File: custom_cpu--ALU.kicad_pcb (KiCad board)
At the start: 2 copper layers, 100 x 60 mm, 25 parts, among them J1 CONN_01X08, J10 CONN_01X01, J11 CONN_01X01, J12 CONN_01X01, J2 CONN_01X08, J3 CONN_01X01, J4 CONN_01X01, J5 CONN_01X08, J6 CONN_01X01, J7 CONN_01X01, J8 CONN_01X01, J9 CONN_01X01, U1 74LS283, U2 74LS283, U3 74LS86, U4 74LS86, U5 74LS245

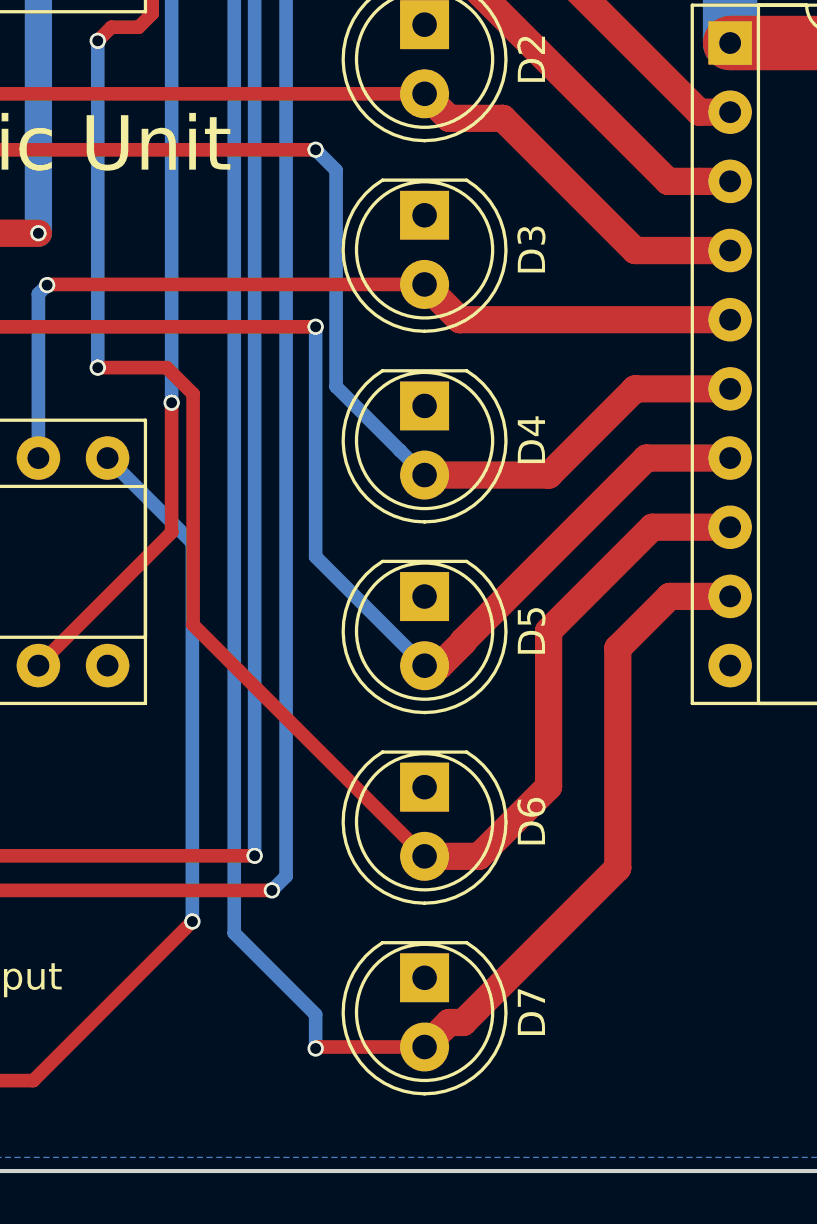
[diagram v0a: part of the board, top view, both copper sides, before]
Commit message: fix a couple more touching traces
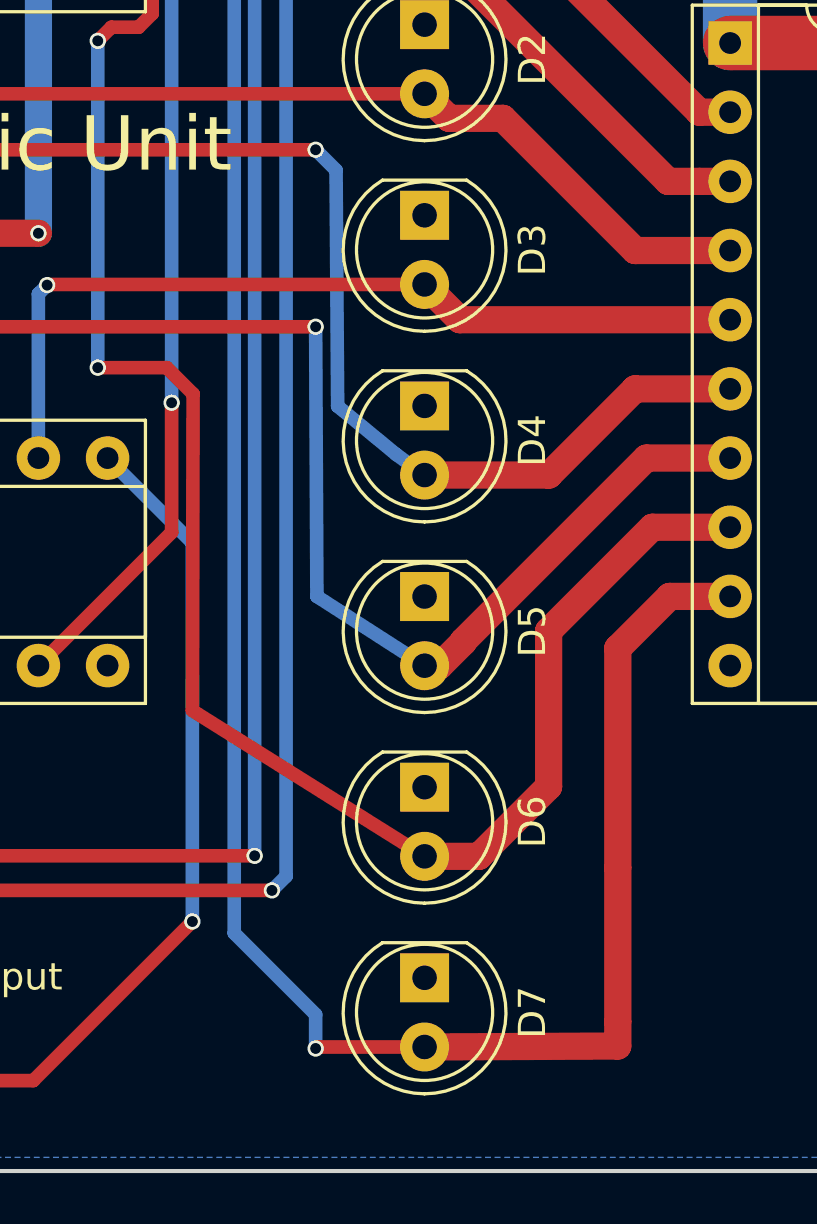
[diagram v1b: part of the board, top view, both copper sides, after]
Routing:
- net Net-(D7-Pad2): track 88.1 -> 91.9 mm
- net Net-(D6-Pad2): track 85.9 -> 87.0 mm
- net Net-(D5-Pad2): track 76.8 -> 77.3 mm
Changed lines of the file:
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@@
-(kicad_pcb (version 4) (host pcbnew 4.0.6-e0-6349~53~ubuntu16.04.1)
+(kicad_pcb (version 4) (host pcbnew 4.0.4+e1-6308~48~ubuntu16.04.1-stable)
   (general
     (links 83)
@@
   )
   (setup
-    (last_trace_width 1)
+    (last_trace_width 0.25)
     (user_trace_width 0.25)
     (user_trace_width 0.5)
@@
   (segment (start 119.295 78.74) (end 129.22 78.74) (width 1) (layer F.Cu) (net 5))
   (segment (start 114 72.5) (end 114.750001 73.250001) (width 0.5) (layer B.Cu) (net 6))
-  (segment (start 114.750001 73.250001) (end 114.750001 81.195001) (width 0.5) (layer B.Cu) (net 6))
-  (segment (start 114.750001 81.195001) (end 117.100001 83.545001) (width 0.5) (layer B.Cu) (net 6))
-  (segment (start 117.100001 83.545001) (end 118 84.445) (width 0.5) (layer B.Cu) (net 6))
+  (segment (start 114.750001 73.250001) (end 114.808 81.915) (width 0.5) (layer B.Cu) (net 6))
+  (segment (start 114.808 81.915) (end 116.967 83.693) (width 0.5) (layer B.Cu) (net 6))
+  (segment (start 116.967 83.693) (end 118 84.445) (width 0.5) (layer B.Cu) (net 6))
   (segment (start 96 73) (end 96.5 72.5) (width 0.5) (layer F.Cu) (net 6))
   (segment (start 96.5 72.5) (end 114 72.5) (width 0.5) (layer F.Cu) (net 6))
@@
   (segment (start 93.5 71) (end 93 70.5) (width 0.5) (layer B.Cu) (net 7))
   (via (at 93 70.5) (size 0.6) (drill 0.4) (layers F.Cu B.Cu) (net 7))
-  (segment (start 118 91.445) (end 114 87.445) (width 0.5) (layer B.Cu) (net 7))
-  (segment (start 114 87.445) (end 114 79) (width 0.5) (layer B.Cu) (net 7))
+  (segment (start 118 91.445) (end 114.046 88.9) (width 0.5) (layer B.Cu) (net 7))
+  (segment (start 114.046 88.9) (end 114 79) (width 0.5) (layer B.Cu) (net 7))
   (via (at 114 79) (size 0.6) (drill 0.4) (layers F.Cu B.Cu) (net 7))
   (segment (start 108 56.5) (end 106 54.5) (width 0.5) (layer B.Cu) (net 8))
@@
   (segment (start 106 80.5) (end 106 68.5) (width 0.5) (layer B.Cu) (net 8))
   (via (at 106 68.5) (size 0.6) (drill 0.4) (layers F.Cu B.Cu) (net 8))
-  (segment (start 109.5 89.945) (end 109.5 81.465998) (width 0.5) (layer F.Cu) (net 8))
+  (segment (start 109.474 93.091) (end 109.5 81.465998) (width 0.5) (layer F.Cu) (net 8))
   (segment (start 109.5 81.465998) (end 108.534002 80.5) (width 0.5) (layer F.Cu) (net 8))
   (segment (start 108.534002 80.5) (end 106 80.5) (width 0.5) (layer F.Cu) (net 8))
   (via (at 106 80.5) (size 0.6) (drill 0.4) (layers F.Cu B.Cu) (net 8))
-  (segment (start 118 98.445) (end 109.5 89.945) (width 0.5) (layer F.Cu) (net 8))
+  (segment (start 118 98.445) (end 109.474 93.091) (width 0.5) (layer F.Cu) (net 8))
   (segment (start 96.266 58.354) (end 96.2 58.42) (width 0.5) (layer B.Cu) (net 8))
   (segment (start 122.555 90.17) (end 126.365 86.36) (width 1) (layer F.Cu) (net 8))
@@
   (segment (start 127 88.9) (end 129.22 88.9) (width 1) (layer F.Cu) (net 9))
   (segment (start 125.095 98.870002) (end 125.095 90.805) (width 1) (layer F.Cu) (net 9))
-  (segment (start 118 105.445) (end 118.899999 104.545001) (width 1) (layer F.Cu) (net 9))
-  (segment (start 118.899999 104.545001) (end 119.420001 104.545001) (width 1) (layer F.Cu) (net 9))
-  (segment (start 119.420001 104.545001) (end 125.095 98.870002) (width 1) (layer F.Cu) (net 9))
+  (segment (start 118 105.445) (end 125.095 105.41) (width 1) (layer F.Cu) (net 9))
+  (segment (start 125.095 105.41) (end 125.095 104.521) (width 1) (layer F.Cu) (net 9))
+  (segment (start 125.095 104.521) (end 125.095 98.870002) (width 1) (layer F.Cu) (net 9))
   (segment (start 66.04 53.34) (end 93.66 53.34) (width 0.5) (layer F.Cu) (net 10))
   (segment (start 93.66 53.34) (end 98.74 58.42) (width 0.5) (layer F.Cu) (net 10))

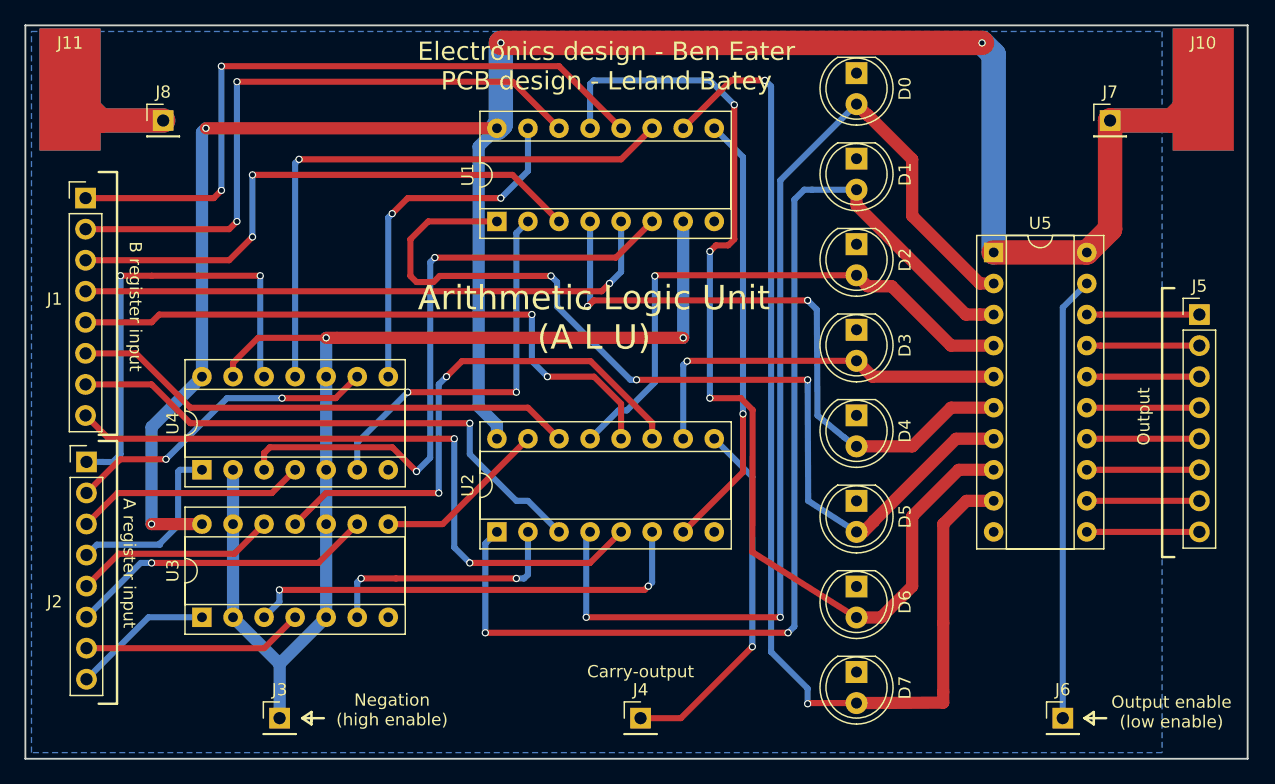
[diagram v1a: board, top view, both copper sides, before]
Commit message: Add power labels
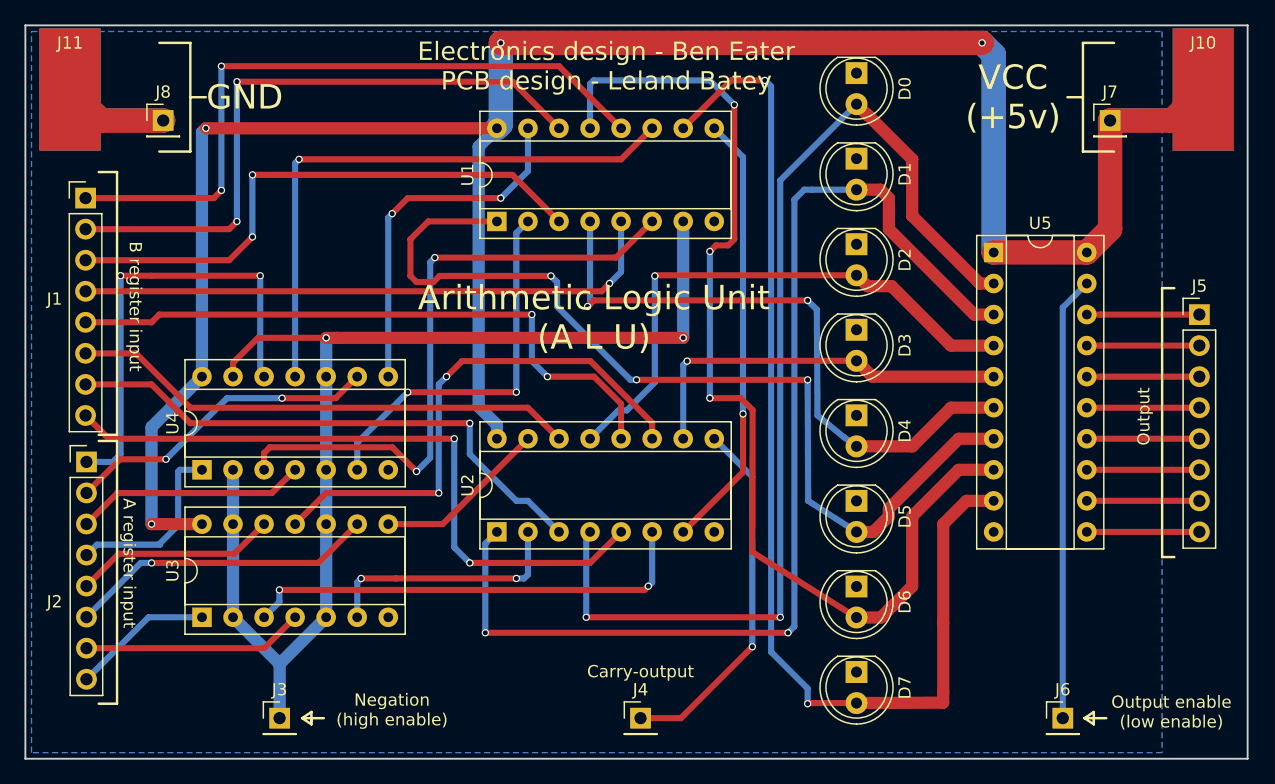
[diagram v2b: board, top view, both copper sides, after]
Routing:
- net Net-(D1-Pad2): track 90.7 -> 91.4 mm
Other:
- board text added: "GND"
- board text added: "VCC (+5v)"
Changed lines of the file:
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@@
-(kicad_pcb (version 4) (host pcbnew 4.0.4+e1-6308~48~ubuntu16.04.1-stable)
+(kicad_pcb (version 4) (host pcbnew 4.0.6-e0-6349~53~ubuntu16.04.1)
   (general
     (links 83)
@@
     (area 48.621667 42.3 168.564286 150.000001)
     (thickness 1.6)
-    (drawings 33)
-    (tracks 356)
+    (drawings 43)
+    (tracks 357)
     (zones 0)
     (modules 25)
@@
       (net 1 GND))
   )
+  (gr_text "VCC\n(+5v)" (at 130.81 55.88) (layer F.SilkS)
+    (effects (font (size 2 2) (thickness 0.4)))
+  )
+  (gr_line (start 136.525 55.88) (end 135.255 55.88) (layer F.SilkS) (width 0.2))
+  (gr_line (start 63.5 55.88) (end 64.77 55.88) (layer F.SilkS) (width 0.2))
+  (gr_line (start 63.5 60.325) (end 63.5 51.435) (layer F.SilkS) (width 0.2))
+  (gr_text GND (at 67.945 55.88) (layer F.SilkS)
+    (effects (font (size 2 2) (thickness 0.4)))
+  )
+  (gr_line (start 63.5 51.435) (end 60.96 51.435) (layer F.SilkS) (width 0.2))
+  (gr_line (start 60.96 60.325) (end 63.5 60.325) (layer F.SilkS) (width 0.2))
+  (gr_line (start 136.525 60.325) (end 139.065 60.325) (layer F.SilkS) (width 0.2))
+  (gr_line (start 136.525 51.435) (end 136.525 60.325) (layer F.SilkS) (width 0.2))
+  (gr_line (start 139.065 51.435) (end 136.525 51.435) (layer F.SilkS) (width 0.2))
   (gr_text "B register input" (at 59 73 270) (layer F.SilkS)
     (effects (font (size 1 1) (thickness 0.2)))
@@
   (segment (start 118 56.445) (end 118.899999 57.344999) (width 1) (layer F.Cu) (net 2))
   (segment (start 118.899999 57.344999) (end 118.939999 57.344999) (width 1) (layer F.Cu) (net 2))
+  (segment (start 120.65 64.135) (end 119.96 63.445) (width 1) (layer F.Cu) (net 3))
+  (segment (start 119.96 63.445) (end 118 63.445) (width 1) (layer F.Cu) (net 3))
+  (segment (start 120.65 66.675) (end 120.65 64.135) (width 1) (layer F.Cu) (net 3))
+  (segment (start 127.635 73.66) (end 120.65 66.675) (width 1) (layer F.Cu) (net 3))
+  (segment (start 129.22 73.66) (end 127.635 73.66) (width 1) (layer F.Cu) (net 3))
   (segment (start 87.63 99.695) (end 87.63 92.39) (width 0.5) (layer B.Cu) (net 3))
   (segment (start 87.63 92.39) (end 88.58 91.44) (width 0.5) (layer B.Cu) (net 3))
@@
   (segment (start 114.355 63.445) (end 113.72 63.445) (width 0.5) (layer B.Cu) (net 3))
   (segment (start 118 63.445) (end 114.355 63.445) (width 0.5) (layer B.Cu) (net 3))
-  (segment (start 118 63.445) (end 118 64.717792) (width 1) (layer F.Cu) (net 3))
-  (segment (start 118 64.717792) (end 126.942208 73.66) (width 1) (layer F.Cu) (net 3))
-  (segment (start 126.942208 73.66) (end 128.08863 73.66) (width 1) (layer F.Cu) (net 3))
-  (segment (start 128.08863 73.66) (end 129.22 73.66) (width 1) (layer F.Cu) (net 3))
   (segment (start 99.209998 81.5) (end 98.52 81.5) (width 0.5) (layer B.Cu) (net 4))
   (segment (start 98.52 81.5) (end 96.2 83.82) (width 0.5) (layer B.Cu) (net 4))
@@
   (segment (start 125.73 81.28) (end 129.22 81.28) (width 1) (layer F.Cu) (net 6))
   (segment (start 118 84.445) (end 122.565 84.445) (width 1) (layer F.Cu) (net 6))
-  (segment (start 129.22 83.82) (end 126.145002 83.82) (width 1) (layer F.Cu) (net 7))
-  (segment (start 126.145002 83.82) (end 119.420001 90.545001) (width 1) (layer F.Cu) (net 7))
-  (segment (start 119.420001 90.545001) (end 119.420001 90.579999) (width 1) (layer F.Cu) (net 7))
-  (segment (start 118.555 91.445) (end 118 91.445) (width 1) (layer F.Cu) (net 7))
-  (segment (start 119.420001 90.579999) (end 118.555 91.445) (width 1) (layer F.Cu) (net 7))
+  (segment (start 129.22 83.82) (end 126.365 83.82) (width 1) (layer F.Cu) (net 7))
+  (segment (start 126.365 83.82) (end 120.65 89.535) (width 1) (layer F.Cu) (net 7))
+  (segment (start 120.65 89.535) (end 120.65 90.17) (width 1) (layer F.Cu) (net 7))
+  (segment (start 120.65 90.17) (end 119.375 91.445) (width 1) (layer F.Cu) (net 7))
+  (segment (start 119.375 91.445) (end 118 91.445) (width 1) (layer F.Cu) (net 7))
   (segment (start 99.5 79) (end 93.5 73) (width 0.5) (layer B.Cu) (net 7))
   (segment (start 93.5 73) (end 93.5 71) (width 0.5) (layer B.Cu) (net 7))
